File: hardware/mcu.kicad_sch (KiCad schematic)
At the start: 22 parts

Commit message: worked on it
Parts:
- C1: renamed from C?; footprint (none) -> Capacitor_SMD:C_0402_1005Metric
- C10, C11: renamed from C?; value C -> 5.6pF; footprint (none) -> Capacitor_SMD:C_0402_1005Metric; Mfr. (none) -> Murata Electronics; Mfr. No (none) -> GRM1555C1H5R6WA01D; Mouser No (none) -> 81-GRM1555C1H5R6WA1D
- C2, C3: renamed from C?; footprint (none) -> Capacitor_SMD:C_0402_1005Metric; Mfr. (none) -> Murata Electronics; Mfr. No (none) -> GJM1555C1H4R7WB01D; Mouser No (none) -> 81-GJM1555C1H4R7WB1D
- C4, C7: renamed from C?; footprint (none) -> Capacitor_SMD:C_0603_1608Metric; Mfr. (none) -> Murata Electronics; Mfr. No (none) -> GRM188Z71A106KA73D; Mouser No (none) -> 81-GRM188Z71A106KA3D
- C5, C8, C9: renamed from C?; footprint (none) -> Capacitor_SMD:C_0402_1005Metric; Mfr. (none) -> Murata Electronics; Mfr. No (none) -> GRM155R71A104KA01D; Mouser No (none) -> 81-GRM155R71A104KA1D
- C6: renamed from C?; footprint (none) -> Capacitor_SMD:C_0402_1005Metric; Mfr. (none) -> Murata Electronics; Mfr. No (none) -> GCM155C71A105KE38D; Mouser No (none) -> 81-GCM155C71A105KE8D
- J1: renamed from J?; footprint (none) -> Connector_PinHeader_1.27mm:PinHeader_2x05_P1.27mm_Vertical
- L1: renamed from L?; footprint (none) -> Inductor_SMD:L_0402_1005Metric
- R4, R6, R7, R8: renamed from R?; footprint (none) -> Resistor_SMD:R_0402_1005Metric
- R5: renamed from R?; footprint (none) -> Resistor_SMD:R_0402_1005Metric; Mfr. (none) -> Vishay / Dale; Mfr. No (none) -> CRCW0402330RJNEDC; Mouser No (none) -> 71-CRCW0402330RJNEDC
- SW1: renamed from SW?; footprint (none) -> Button_Switch_SMD:SW_SPST_B3U-1000P; Mfr. (none) -> Omron Electronics; Mfr. No (none) -> B3U-1000P; Mouser No (none) -> 653-B3U-1000P
- U1: renamed from U?; Mfr. (none) -> Microchip Technology / Atmel; Mfr. No (none) -> ATSAMC21E16A-ANT; Mouser No (none) -> 556-ATSAMC21E16A-ANT
- Y1: renamed from Y?; footprint (none) -> Crystal:Crystal_SMD_3215-2Pin_3.2x1.5mm; Mfr. (none) -> ABRACON; Mfr. No (none) -> ABS07-32.768KHZ-7-T; Mouser No (none) -> 815-ABS07-32.768K7T
- Y2: renamed from Y?; footprint (none) -> Crystal:Crystal_SMD_2016-4Pin_2.0x1.6mm; Mfr. (none) -> ABRACON; Mfr. No (none) -> ABM11W-32.0000MHZ-8-D1X-T3; Mouser No (none) -> 815-11W32-8D1XT

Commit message: picked parts
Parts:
- C1: Mfr. (none) -> Murata Electronics; Mfr. No (none) -> GRM1555C1H101JA01D; Mouser No (none) -> 81-GRM1555C1H101JA1D
- L1: footprint Inductor_SMD:L_0402_1005Metric -> Inductor_SMD:L_0805_2012Metric; Mfr. (none) -> Bourns; Mfr. No (none) -> CE201210-39NJ; Mouser No (none) -> 652-CE201210-39NJ
- R4: Mfr. (none) -> YAGEO; Mfr. No (none) -> RC0402FR-072K2L; Mouser No (none) -> 603-RC0402FR-072K2L
- R6, R7: Mfr. (none) -> YAGEO; Mfr. No (none) -> RC0402FR-0733KL; Mouser No (none) -> 603-RC0402FR-0733KL
- R8: Mfr. (none) -> YAGEO; Mfr. No (none) -> RC0402FR-0722RL; Mouser No (none) -> 603-RC0402FR-0722RL
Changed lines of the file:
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@@
       (effects (font (size 1.27 1.27)) hide)
     )
-    (property "Datasheet" "~" (id 3) (at 213.36 134.62 0)
+    (property "Datasheet" "./datasheets/PYu_RC_Group_51_RoHS_L_11-1984063.pdf" (id 3) (at 213.36 134.62 0)
+      (effects (font (size 1.27 1.27)) hide)
+    )
+    (property "Mfr." "YAGEO" (id 4) (at 213.36 134.62 0)
+      (effects (font (size 1.27 1.27)) hide)
+    )
+    (property "Mfr. No" "RC0402FR-0722RL" (id 5) (at 213.36 134.62 0)
+      (effects (font (size 1.27 1.27)) hide)
+    )
+    (property "Mouser No" "603-RC0402FR-0722RL" (id 6) (at 213.36 134.62 0)
       (effects (font (size 1.27 1.27)) hide)
     )
@@
       (effects (font (size 1.27 1.27)) hide)
     )
-    (property "Datasheet" "~" (id 3) (at 191.77 120.65 0)
+    (property "Datasheet" "./datasheets/PYu_RC_Group_51_RoHS_L_11-1984063.pdf" (id 3) (at 191.77 120.65 0)
+      (effects (font (size 1.27 1.27)) hide)
+    )
+    (property "Mfr." "YAGEO" (id 4) (at 191.77 120.65 0)
+      (effects (font (size 1.27 1.27)) hide)
+    )
+    (property "Mfr. No" "RC0402FR-0733KL" (id 5) (at 191.77 120.65 0)
+      (effects (font (size 1.27 1.27)) hide)
+    )
+    (property "Mouser No" "603-RC0402FR-0733KL" (id 6) (at 191.77 120.65 0)
       (effects (font (size 1.27 1.27)) hide)
     )
@@
       (effects (font (size 1.27 1.27)) hide)
     )
-    (property "Datasheet" "~" (id 3) (at 60.96 69.85 0)
+    (property "Datasheet" "./datasheets/GRM1555C1H101JA01_01A-1982687.pdf" (id 3) (at 60.96 69.85 0)
+      (effects (font (size 1.27 1.27)) hide)
+    )
+    (property "Mfr." "Murata Electronics" (id 4) (at 60.96 69.85 0)
+      (effects (font (size 1.27 1.27)) hide)
+    )
+    (property "Mfr. No" "GRM1555C1H101JA01D" (id 5) (at 60.96 69.85 0)
+      (effects (font (size 1.27 1.27)) hide)
+    )
+    (property "Mouser No" "81-GRM1555C1H101JA1D" (id 6) (at 60.96 69.85 0)
       (effects (font (size 1.27 1.27)) hide)
     )
@@
     (property "Reference" "L1" (id 0) (at 102.87 54.61 90))
     (property "Value" "39nH" (id 1) (at 102.87 57.15 90))
-    (property "Footprint" "Inductor_SMD:L_0402_1005Metric" (id 2) (at 102.87 60.96 0)
-      (effects (font (size 1.27 1.27)) hide)
-    )
-    (property "Datasheet" "~" (id 3) (at 102.87 60.96 0)
+    (property "Footprint" "Inductor_SMD:L_0805_2012Metric" (id 2) (at 102.87 60.96 0)
+      (effects (font (size 1.27 1.27)) hide)
+    )
+    (property "Datasheet" "./datasheets/ce201210-777343.pdf" (id 3) (at 102.87 60.96 0)
+      (effects (font (size 1.27 1.27)) hide)
+    )
+    (property "Mfr." "Bourns" (id 4) (at 102.87 60.96 0)
+      (effects (font (size 1.27 1.27)) hide)
+    )
+    (property "Mfr. No" "CE201210-39NJ" (id 5) (at 102.87 60.96 0)
+      (effects (font (size 1.27 1.27)) hide)
+    )
+    (property "Mouser No" "652-CE201210-39NJ" (id 6) (at 102.87 60.96 0)
       (effects (font (size 1.27 1.27)) hide)
     )
@@
       (effects (font (size 1.27 1.27)) hide)
     )
-    (property "Datasheet" "~" (id 3) (at 207.01 120.65 0)
+    (property "Datasheet" "./datasheets/PYu_RC_Group_51_RoHS_L_11-1984063.pdf" (id 3) (at 207.01 120.65 0)
+      (effects (font (size 1.27 1.27)) hide)
+    )
+    (property "Mfr." "YAGEO" (id 4) (at 207.01 120.65 0)
+      (effects (font (size 1.27 1.27)) hide)
+    )
+    (property "Mfr. No" "RC0402FR-0733KL" (id 5) (at 207.01 120.65 0)
+      (effects (font (size 1.27 1.27)) hide)
+    )
+    (property "Mouser No" "603-RC0402FR-0733KL" (id 6) (at 207.01 120.65 0)
       (effects (font (size 1.27 1.27)) hide)
     )
@@
       (effects (font (size 1.27 1.27)) hide)
     )
-    (property "Datasheet" "~" (id 3) (at 48.26 69.85 0)
-      (effects (font (size 1.27 1.27)) hide)
-    )
+    (property "Datasheet" "./datasheets/PYu_RC_Group_51_RoHS_L_11-1984063.pdf" (id 3) (at 48.26 69.85 0)
+      (effects (font (size 1.27 1.27)) hide)
+    )
+    (property "Mfr." "YAGEO" (id 4) (at 48.26 69.85 0)
+      (effects (font (size 1.27 1.27)) hide)
+    )
+    (property "Mfr. No" "RC0402FR-072K2L" (id 5) (at 48.26 69.85 0)
+      (effects (font (size 1.27 1.27)) hide)
+    )
+    (property "Mouser No" "603-RC0402FR-072K2L" (id 6) (at 48.26 69.85 0)
+      (effects (font (size 1.27 1.27)) hide)
+    )

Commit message: ordered, pray this works
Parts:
- J1: footprint Connector_PinHeader_1.27mm:PinHeader_2x05_P1.27mm_Vertical -> sam-fd:PinHeader_2x05_P1.27mm_Vertical
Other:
- company: (none) -> Leon Rinkel
- title: (none) -> sam-fd
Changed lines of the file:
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@@
 (kicad_sch (version 20211123) (generator eeschema)
   (paper "A4")
+  (title_block
+    (title "sam-fd")
+    (date "2023-01-27")
+    (rev "2")
+    (company "Leon Rinkel")
+    (comment 1 "leon@rinkel.me")
+    (comment 2 "https://git.leon.fyi/leonrinkel/sam-fd")
+  )
   (junction (at 191.77 132.08) (diameter 0) (color 0 0 0 0)
   )
@@
       (effects (font (size 1.27 1.27)) (justify right))
     )
-    (property "Footprint" "Connector_PinHeader_1.27mm:PinHeader_2x05_P1.27mm_Vertical" (id 2) (at 232.41 134.62 0)
+    (property "Footprint" "sam-fd:PinHeader_2x05_P1.27mm_Vertical" (id 2) (at 232.41 134.62 0)
       (effects (font (size 1.27 1.27)) hide)
     )
@@
       (effects (font (size 1.27 1.27)) hide)
     )
-    (property "Datasheet" "./datasheets/SAM_C20_C21_Family_Data_Sheet_DS60001479J-2902525.pdf" (id 3) (at 137.16 130.81 0)
-      (effects (font (size 1.27 1.27)) hide)
-    )
+    (property "Datasheet" "./datasheets/SAM-C20-C21-Family-Data-Sheet-DS60001479J.pdf" (id 3) (at 137.16 130.81 0)
+      (effects (font (size 1.27 1.27)) hide)
+    )

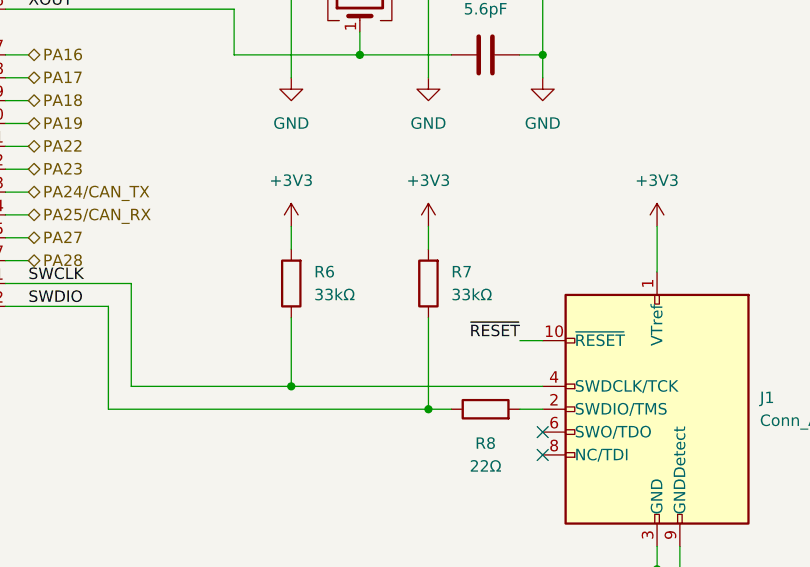
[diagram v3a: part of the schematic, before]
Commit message: leds through transistor, castellated holes
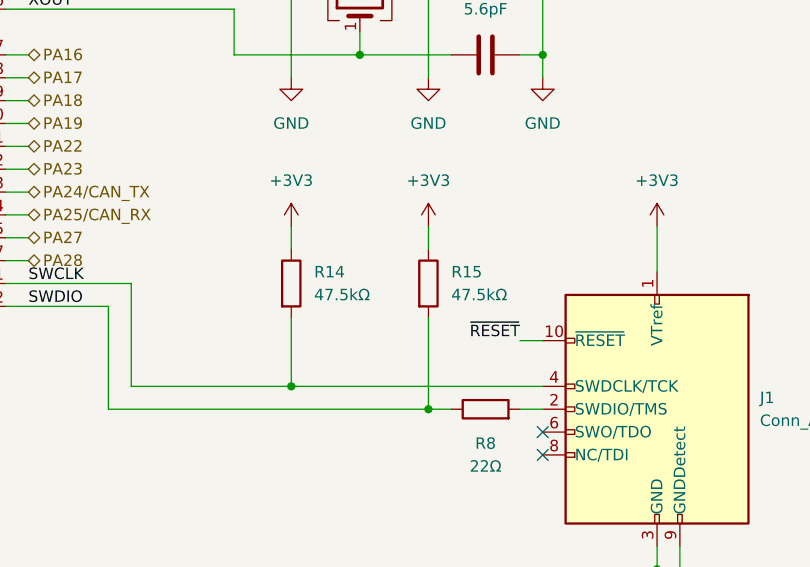
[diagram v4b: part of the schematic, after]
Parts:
- removed R6, R7: 33kΩ, Resistor_SMD:R_0402_1005Metric, symbol Device:R
- added R14, R15: 47.5kΩ, Resistor_SMD:R_0402_1005Metric, symbol Device:R
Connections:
- net +3V3: now also R14.1, R15.1
- net SWCLK: now also R14.2
- net SWDIO: now also R15.2
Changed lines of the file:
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@@
     (title "sam-fd")
     (date "2023-01-27")
-    (rev "2")
+    (rev "3")
     (company "Leon Rinkel")
     (comment 1 "leon@rinkel.me")
@@
     )
     (pin "1")
+  )
+  (symbol (lib_id "Device:R") (at 207.01 120.65 0) (unit 1)
+    (in_bom yes) (on_board yes) (fields_autoplaced)
+    (property "Reference" "R15" (id 0) (at 209.55 119.3799 0)
+      (effects (font (size 1.27 1.27)) (justify left))
+    )
+    (property "Value" "47.5kΩ" (id 1) (at 209.55 121.9199 0)
+      (effects (font (size 1.27 1.27)) (justify left))
+    )
+    (property "Footprint" "Resistor_SMD:R_0402_1005Metric" (id 2) (at 205.232 120.65 90)
+      (effects (font (size 1.27 1.27)) hide)
+    )
+    (property "Datasheet" "./datasheets/crcwce3-1762584.pdf" (id 3) (at 207.01 120.65 0)
+      (effects (font (size 1.27 1.27)) hide)
+    )
+    (property "Mfr." "Vishay / Dale" (id 4) (at 207.01 120.65 0)
+      (effects (font (size 1.27 1.27)) hide)
+    )
+    (property "Mfr. No" "CRCW040247K5FKEDC" (id 5) (at 207.01 120.65 0)
+      (effects (font (size 1.27 1.27)) hide)
+    )
+    (property "Mouser No" "71-CRCW040247K5FKEDC" (id 6) (at 207.01 120.65 0)
+      (effects (font (size 1.27 1.27)) hide)
+    )
+    (pin "1")
+    (pin "2")
   )
   (symbol (lib_id "Connector:Conn_ARM_JTAG_SWD_10") (at 232.41 134.62 0) (mirror y) (unit 1)
@@
     (pin "1")
   )
-  (symbol (lib_id "Device:R") (at 191.77 120.65 180) (unit 1)
-    (in_bom yes) (on_board yes) (fields_autoplaced)
-    (property "Reference" "R6" (id 0) (at 194.31 119.3799 0)
-      (effects (font (size 1.27 1.27)) (justify right))
-    )
-    (property "Value" "33kΩ" (id 1) (at 194.31 121.9199 0)
-      (effects (font (size 1.27 1.27)) (justify right))
-    )
-    (property "Footprint" "Resistor_SMD:R_0402_1005Metric" (id 2) (at 193.548 120.65 90)
-      (effects (font (size 1.27 1.27)) hide)
-    )
-    (property "Datasheet" "./datasheets/PYu_RC_Group_51_RoHS_L_11-1984063.pdf" (id 3) (at 191.77 120.65 0)
-      (effects (font (size 1.27 1.27)) hide)
-    )
-    (property "Mfr." "YAGEO" (id 4) (at 191.77 120.65 0)
-      (effects (font (size 1.27 1.27)) hide)
-    )
-    (property "Mfr. No" "RC0402FR-0733KL" (id 5) (at 191.77 120.65 0)
-      (effects (font (size 1.27 1.27)) hide)
-    )
-    (property "Mouser No" "603-RC0402FR-0733KL" (id 6) (at 191.77 120.65 0)
-      (effects (font (size 1.27 1.27)) hide)
-    )
-    (pin "1")
-    (pin "2")
-  )
   (symbol (lib_id "Device:C") (at 165.1 67.31 0) (unit 1)
     (in_bom yes) (on_board yes) (fields_autoplaced)
@@
     (pin "1")
   )
+  (symbol (lib_id "Device:R") (at 191.77 120.65 0) (unit 1)
+    (in_bom yes) (on_board yes) (fields_autoplaced)
+    (property "Reference" "R14" (id 0) (at 194.31 119.3799 0)
+      (effects (font (size 1.27 1.27)) (justify left))
+    )
+    (property "Value" "47.5kΩ" (id 1) (at 194.31 121.9199 0)
+      (effects (font (size 1.27 1.27)) (justify left))
+    )
+    (property "Footprint" "Resistor_SMD:R_0402_1005Metric" (id 2) (at 189.992 120.65 90)
+      (effects (font (size 1.27 1.27)) hide)
+    )
+    (property "Datasheet" "./datasheets/crcwce3-1762584.pdf" (id 3) (at 191.77 120.65 0)
+      (effects (font (size 1.27 1.27)) hide)
+    )
+    (property "Mfr." "Vishay / Dale" (id 4) (at 191.77 120.65 0)
+      (effects (font (size 1.27 1.27)) hide)
+    )
+    (property "Mfr. No" "CRCW040247K5FKEDC" (id 5) (at 191.77 120.65 0)
+      (effects (font (size 1.27 1.27)) hide)
+    )
+    (property "Mouser No" "71-CRCW040247K5FKEDC" (id 6) (at 191.77 120.65 0)
+      (effects (font (size 1.27 1.27)) hide)
+    )
+    (pin "1")
+    (pin "2")
+  )
   (symbol (lib_id "Device:Crystal_GND24") (at 199.39 88.9 90) (unit 1)
     (in_bom yes) (on_board yes) (fields_autoplaced)
@@
     (pin "2")
   )
-  (symbol (lib_id "Device:R") (at 207.01 120.65 180) (unit 1)
-    (in_bom yes) (on_board yes) (fields_autoplaced)
-    (property "Reference" "R7" (id 0) (at 209.55 119.3799 0)
-      (effects (font (size 1.27 1.27)) (justify right))
-    )
-    (property "Value" "33kΩ" (id 1) (at 209.55 121.9199 0)
-      (effects (font (size 1.27 1.27)) (justify right))
-    )
-    (property "Footprint" "Resistor_SMD:R_0402_1005Metric" (id 2) (at 208.788 120.65 90)
-      (effects (font (size 1.27 1.27)) hide)
-    )
-    (property "Datasheet" "./datasheets/PYu_RC_Group_51_RoHS_L_11-1984063.pdf" (id 3) (at 207.01 120.65 0)
-      (effects (font (size 1.27 1.27)) hide)
-    )
-    (property "Mfr." "YAGEO" (id 4) (at 207.01 120.65 0)
-      (effects (font (size 1.27 1.27)) hide)
-    )
-    (property "Mfr. No" "RC0402FR-0733KL" (id 5) (at 207.01 120.65 0)
-      (effects (font (size 1.27 1.27)) hide)
-    )
-    (property "Mouser No" "603-RC0402FR-0733KL" (id 6) (at 207.01 120.65 0)
-      (effects (font (size 1.27 1.27)) hide)
-    )
-    (pin "1")
-    (pin "2")
-  )
   (symbol (lib_id "Device:R") (at 48.26 69.85 0) (unit 1)
     (in_bom yes) (on_board yes) (fields_autoplaced)
@@
       (effects (font (size 1.27 1.27)) hide)
     )
-    (property "Datasheet" "./datasheets/SAM-C20-C21-Family-Data-Sheet-DS60001479J.pdf" (id 3) (at 137.16 130.81 0)
-      (effects (font (size 1.27 1.27)) hide)
-    )
+    (property "Datasheet" "./datasheets/SAM_C20_C21_Family_Data_Sheet_DS60001479J-2902525.pdf" (id 3) (at 137.16 130.81 0)
+      (effects (font (size 1.27 1.27)) hide)
+    )
